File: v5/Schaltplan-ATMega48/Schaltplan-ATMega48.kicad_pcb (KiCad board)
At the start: 2 copper layers, 18 parts, among them J1 AVR-ISP-6, SW1 SW_Push, SW2 SW_Push, SW3 SW_Push, U1 ATmega48A-P, Y1 Crystal_Small

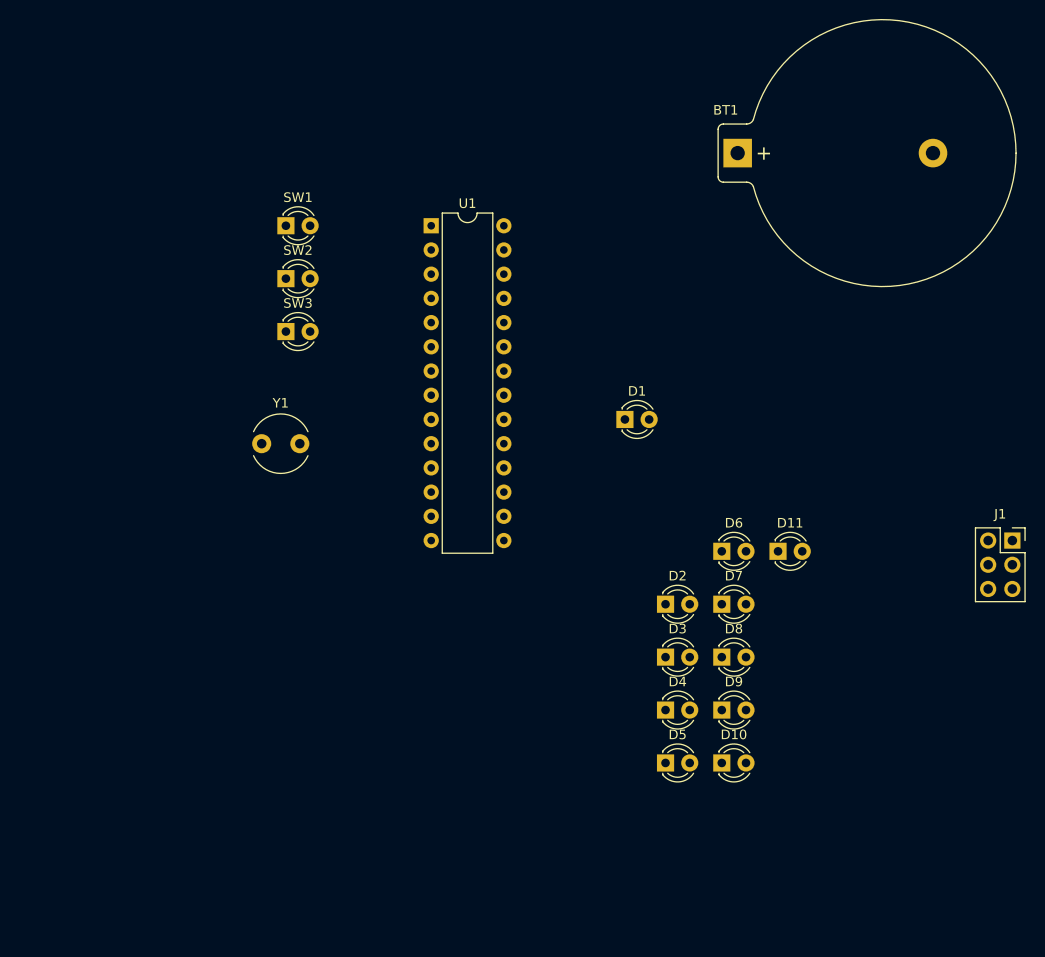
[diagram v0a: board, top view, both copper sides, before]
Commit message: Add SRC and DRC for PCB layout, rearrange stuff
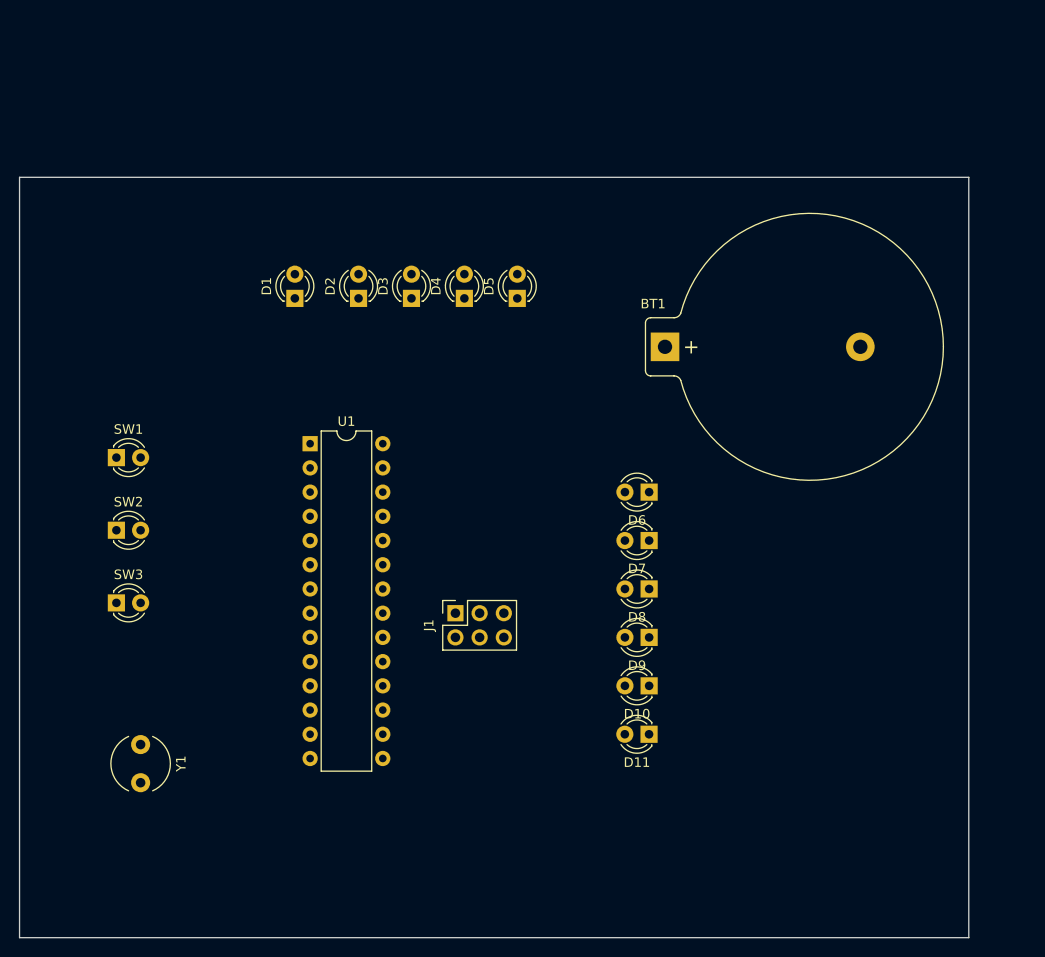
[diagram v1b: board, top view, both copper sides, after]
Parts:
- moved J1 58.9 mm to (96.5, 96.5), turned to 90 degrees
- moved D5 51.2 mm to (103.0, 63.5), turned to 90 degrees
- moved D4 48.1 mm to (97.5, 63.5), turned to 90 degrees
- moved D3 46.1 mm to (91.9, 63.5), turned to 90 degrees
- moved D2 45.5 mm to (86.4, 63.5), turned to 90 degrees
- moved D1 36.9 mm to (79.7, 63.5), turned to 90 degrees
- moved Y1 34.0 mm to (63.5, 110.3), turned to -90 degrees
- moved SW3 33.6 mm to (61.0, 95.4)
- moved SW2 31.8 mm to (61.0, 87.8)
- moved SW1 30.1 mm to (61.0, 80.2)
- moved U1 26.2 mm to (81.3, 78.7)
- moved D11 23.5 mm to (116.8, 109.2), turned to 180 degrees
- moved BT1 21.7 mm to (118.5, 68.6)
- moved D10 11.1 mm to (116.8, 104.1), turned to 180 degrees
- moved D9 10.8 mm to (116.8, 99.1), turned to 180 degrees
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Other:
- board outline added: 99.6 x 79.8 mm

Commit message: update pcb correctly
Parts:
- moved J1 2.54 mm to (96.5, 94.0)
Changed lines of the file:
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@@
   (net 27 "Net-(J1-MISO)")
   (footprint "Connector_PinSocket_2.54mm:PinSocket_2x03_P2.54mm_Vertical" (layer "F.Cu")
-    (at 96.52 96.52 90)
+    (at 96.52 93.98 90)
     (descr "Through hole straight socket strip, 2x03, 2.54mm pitch, double cols (from Kicad 4.0.7), script generated")
     (tags "Through hole socket strip THT 2x03 2.54mm double row")

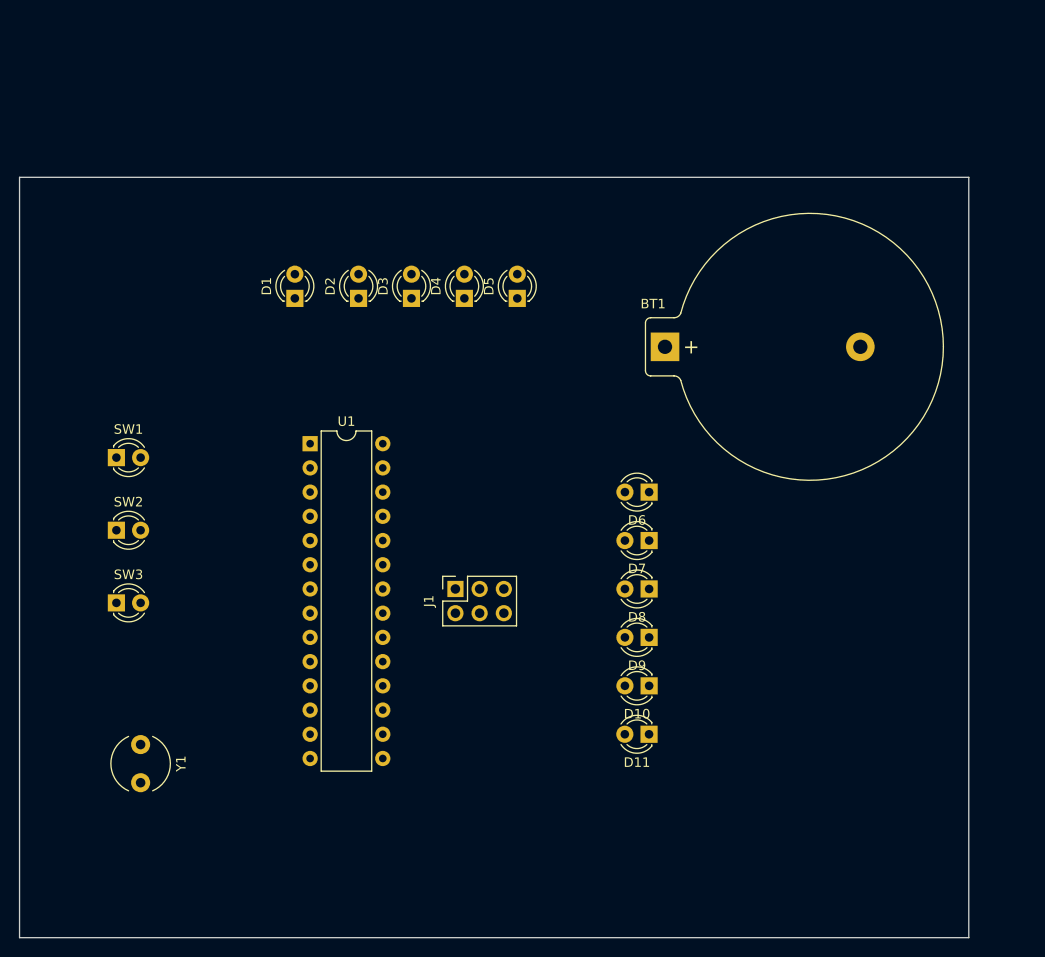
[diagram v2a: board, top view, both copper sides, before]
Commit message: first finalization of Platine, DRC errors yet to be fixed
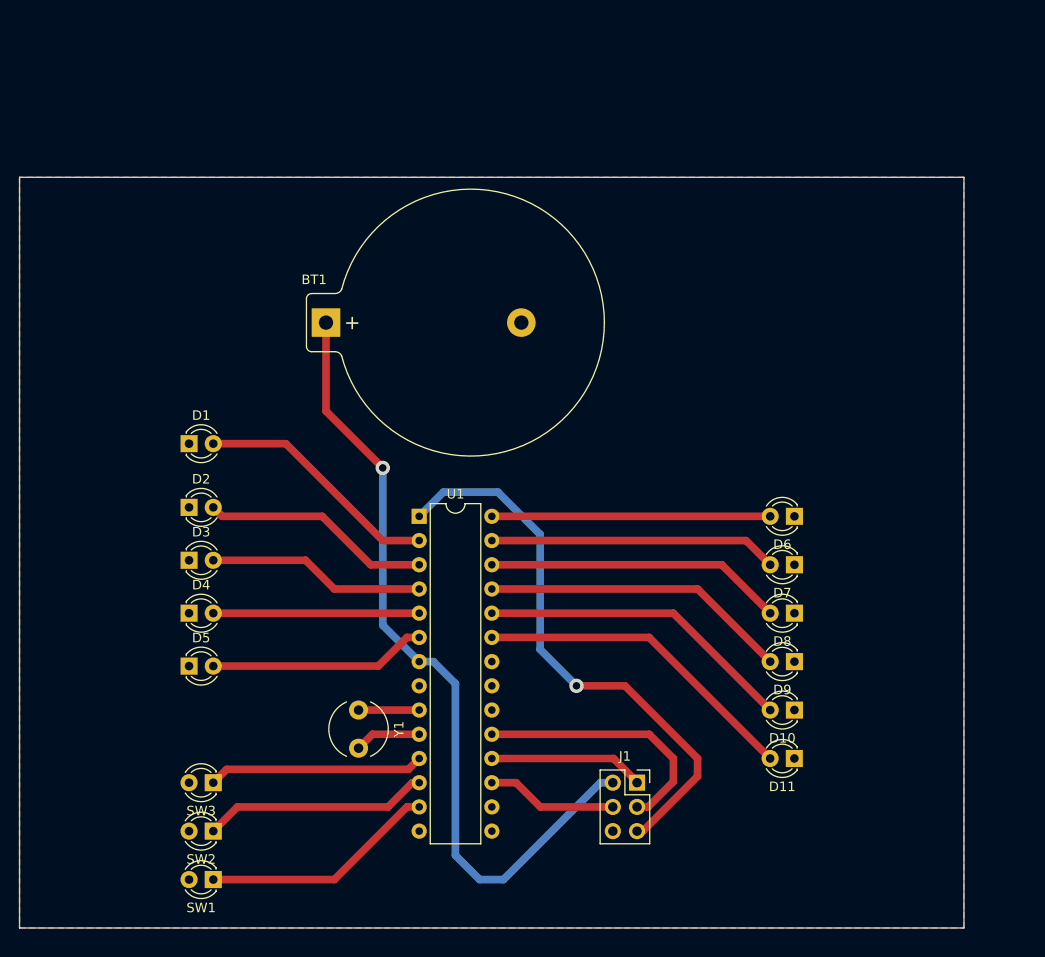
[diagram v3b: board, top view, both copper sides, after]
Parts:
- moved D5 51.7 mm to (68.6, 102.1), turned to 0 degrees
- moved SW1 45.4 mm to (71.1, 124.5), turned to 180 degrees
- moved D4 43.9 mm to (68.6, 96.5), turned to 0 degrees
- moved D3 36.0 mm to (68.6, 91.0), turned to 0 degrees
- moved BT1 35.7 mm to (82.9, 66.0)
- moved SW2 33.2 mm to (71.1, 119.4), turned to 180 degrees
- moved D2 28.2 mm to (68.6, 85.4), turned to 0 degrees
- moved J1 27.9 mm to (115.6, 114.3), turned to 0 degrees
- moved Y1 23.1 mm to (86.4, 106.7)
- moved SW3 21.4 mm to (71.1, 114.3), turned to 180 degrees
- moved D1 18.9 mm to (68.6, 78.7), turned to 0 degrees
- moved D10 15.5 mm to (132.1, 106.7)
- moved D6 15.5 mm to (132.1, 86.4)
- moved D7 15.5 mm to (132.1, 91.4)
- moved D8 15.5 mm to (132.1, 96.5)
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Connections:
- SW1 pad 1: Net-(U1-PD2) -> Net-(U1-PD7)
- SW2 pad 1: Net-(U1-PD3) -> Net-(U1-PD6)
- SW3 pad 1: Net-(U1-PD4) -> Net-(U1-PD5)
- U1 pad 11: unconnected-(U1-PD5-Pad11) -> Net-(U1-PD5)
- U1 pad 12: unconnected-(U1-PD6-Pad12) -> Net-(U1-PD6)
- U1 pad 13: unconnected-(U1-PD7-Pad13) -> Net-(U1-PD7)
- U1 pad 14: Net-(D11-A) -> unconnected-(U1-PB0-Pad14)
- U1 pad 15: Net-(D10-A) -> unconnected-(U1-PB1-Pad15)
- U1 pad 16: Net-(D9-A) -> unconnected-(U1-PB2-Pad16)
- U1 pad 2: Net-(D2-A) -> Net-(D1-A)
- U1 pad 23: Net-(D8-A) -> Net-(D11-A)
- U1 pad 24: Net-(D7-A) -> Net-(D10-A)
- U1 pad 25: Net-(D6-A) -> Net-(D9-A)
- U1 pad 26: Net-(D5-A) -> Net-(D8-A)
- U1 pad 27: Net-(D4-A) -> Net-(D7-A)
- U1 pad 28: Net-(D3-A) -> Net-(D6-A)
- U1 pad 3: Net-(D1-A) -> Net-(D2-A)
- U1 pad 4: Net-(U1-PD2) -> Net-(D3-A)
- U1 pad 5: Net-(U1-PD3) -> Net-(D4-A)
- U1 pad 6: Net-(U1-PD4) -> Net-(D5-A)
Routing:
- net Net-(BT1-+): track 0.00 -> 84.1 mm, vias 0 -> 1
- net Net-(J1-~{RST}): track 0.00 -> 59.5 mm, vias 0 -> 1
- net Net-(D11-A): track 0.00 -> 34.5 mm
- net Net-(D10-A): track 0.00 -> 33.4 mm
- net Net-(D9-A): track 0.00 -> 32.4 mm
- net Net-(D8-A): track 0.00 -> 31.3 mm
- net Net-(D7-A): track 0.00 -> 30.3 mm
- net Net-(D6-A): track 0.00 -> 29.2 mm
- net Net-(J1-SCK): track 0.00 -> 27.4 mm
- net Net-(D1-A): track 0.00 -> 25.8 mm
- net Net-(U1-PD7): track 0.00 -> 24.9 mm
- net Net-(D2-A): track 0.00 -> 24.1 mm
- net Net-(U1-PD6): track 0.00 -> 23.7 mm
- net Net-(D3-A): track 0.00 -> 22.8 mm
- net Net-(D5-A): track 0.00 -> 22.8 mm
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- added copper zone on B.Cu, net GNDREF
- added copper zone on F.Cu, net GNDREF
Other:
- board size 99.6 x 79.8 mm -> 99.1 x 78.7 mm

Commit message: Rework PCB so that only blue lines connecting to BAT, ATMega and ISP
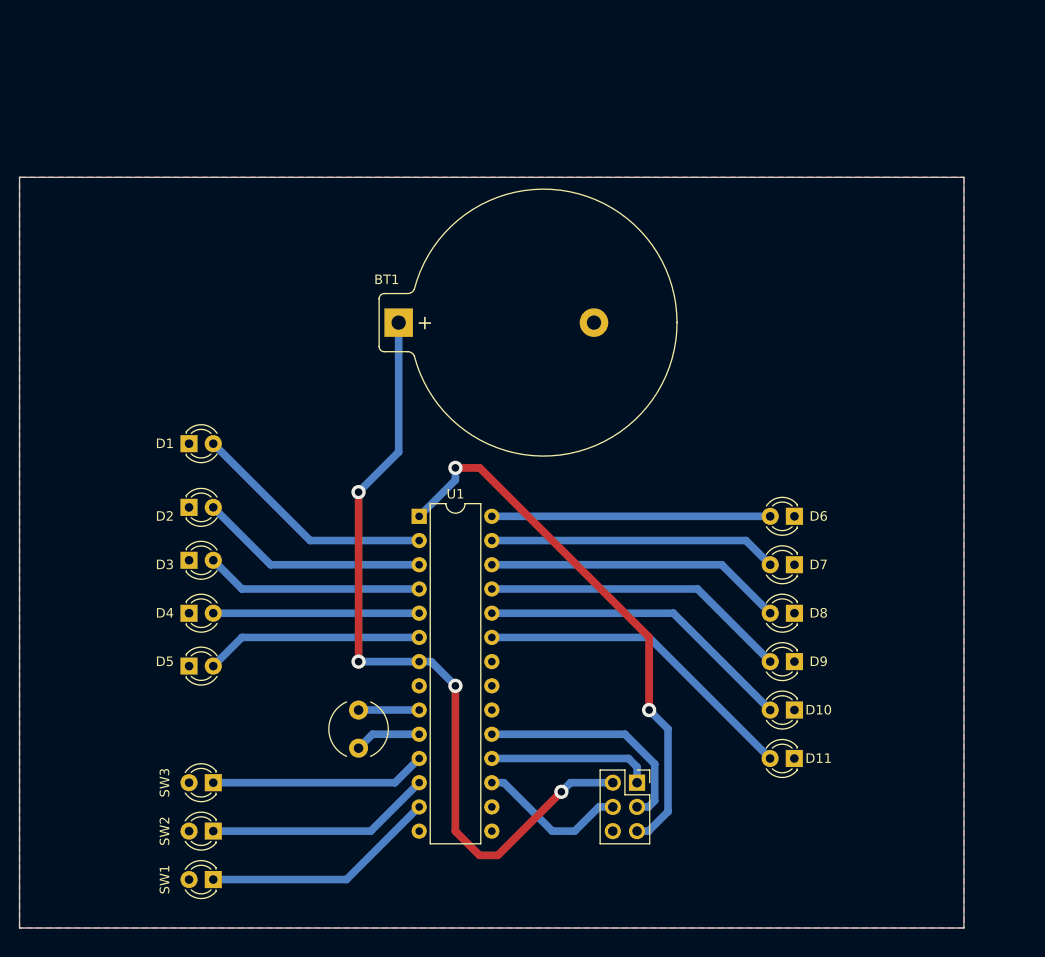
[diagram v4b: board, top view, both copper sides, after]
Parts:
- moved BT1 7.62 mm to (90.6, 66.0)
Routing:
- net Net-(J1-SCK): track 27.4 -> 24.3 mm
- net Net-(J1-MOSI): track 13.7 -> 15.8 mm
- net Net-(J1-~{RST}): track 59.5 -> 57.5 mm, vias 1 -> 2
- net Net-(J1-MISO): track 16.3 -> 17.3 mm
- net Net-(BT1-+): track 84.1 -> 84.5 mm, vias 1 -> 4
